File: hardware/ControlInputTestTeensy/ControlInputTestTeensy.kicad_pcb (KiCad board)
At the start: 2 copper layers, 88.9 x 66 mm, 11 parts, among them J1 RC, J13 Main Power, J4 Power Input, J5 I2C, J7 8P8C, U1 Teensy4.0_NoMid, U3 OLED Feather

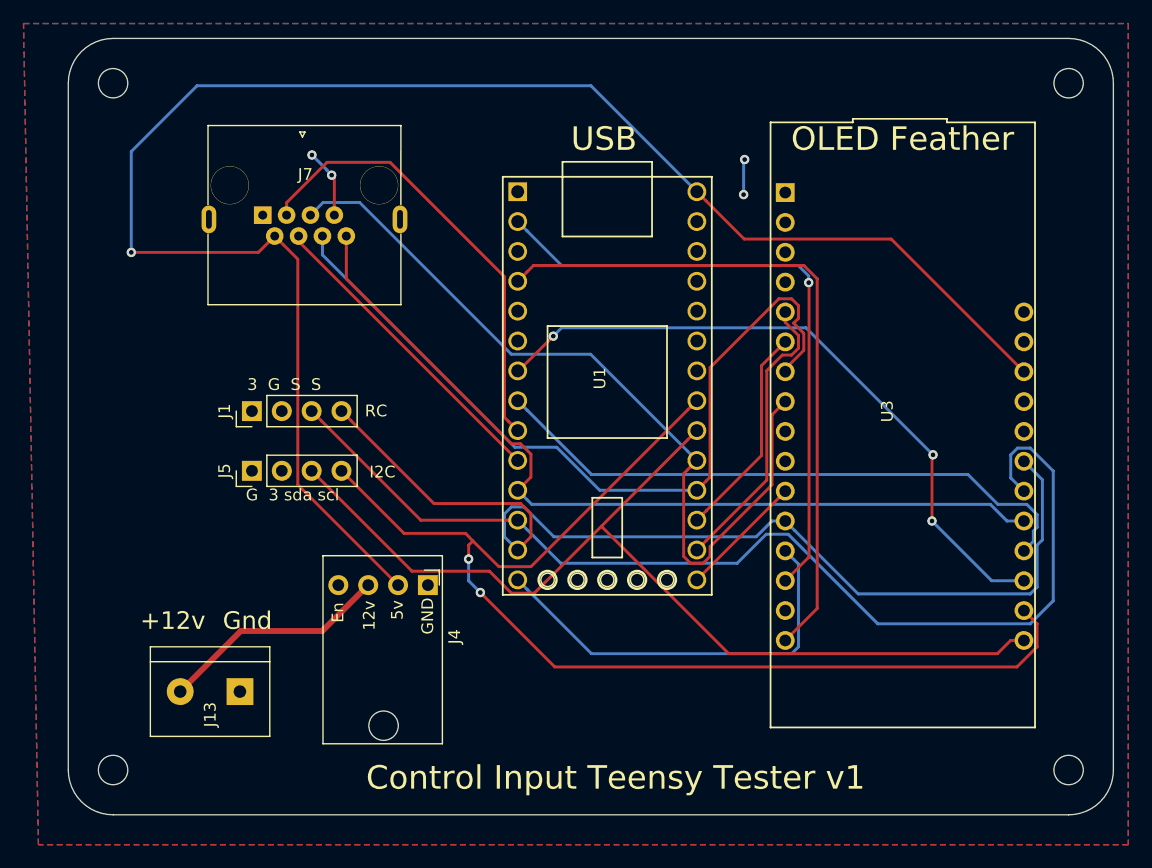
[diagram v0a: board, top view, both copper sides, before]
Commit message: tweaks to Control Input for Teensy PCB
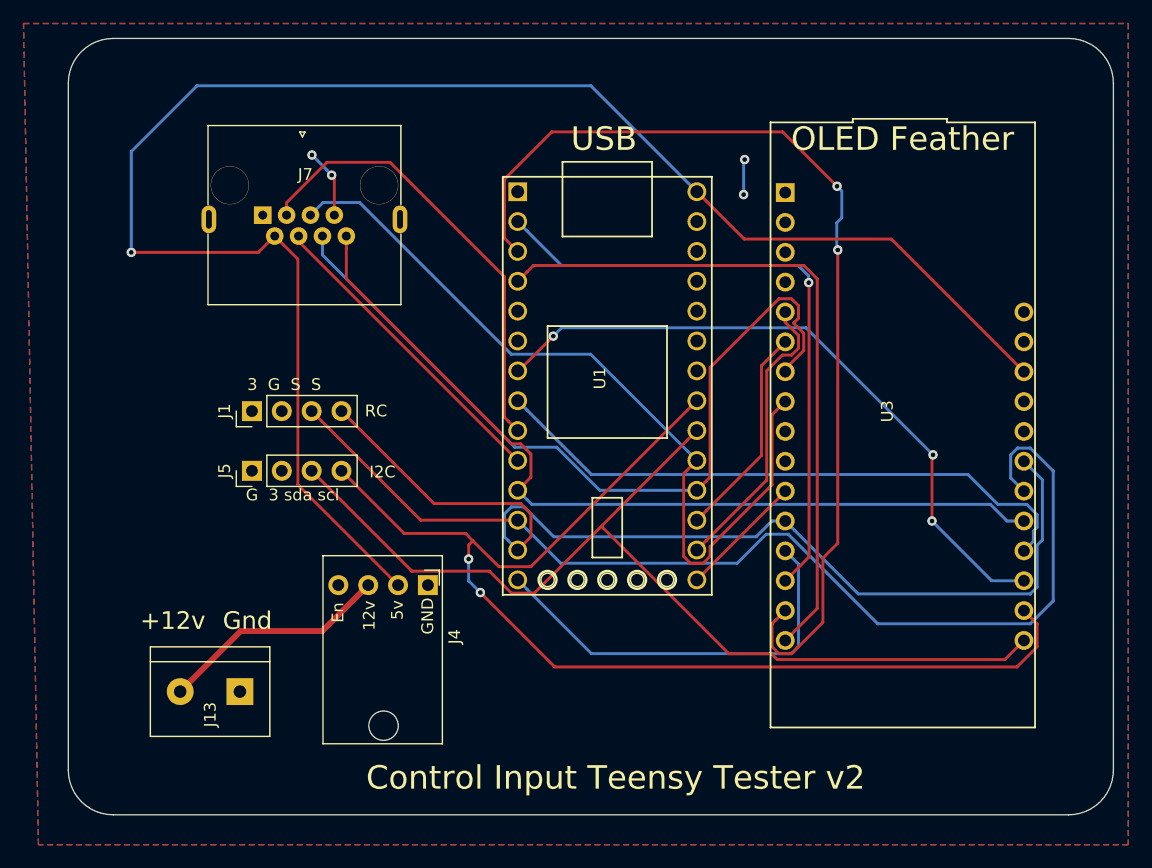
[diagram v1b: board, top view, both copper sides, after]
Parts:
- removed REF** (x4): MountingHole_2.5mm, MountingHole:MountingHole_2.5mm
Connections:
- U1 pad 3: Net-(U1-Pad3) -> TX
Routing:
- net TX: track 0.00 -> 85.7 mm, vias 0 -> 2
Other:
- board text added: "Control Input Teensy Tester v2"
- board text removed: "Control Input Teensy Tester v1"
